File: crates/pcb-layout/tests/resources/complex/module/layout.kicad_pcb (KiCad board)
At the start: 2 copper layers, 4 parts

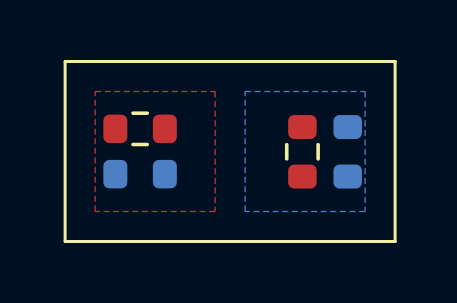
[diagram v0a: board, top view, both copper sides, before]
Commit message: add more interesting test
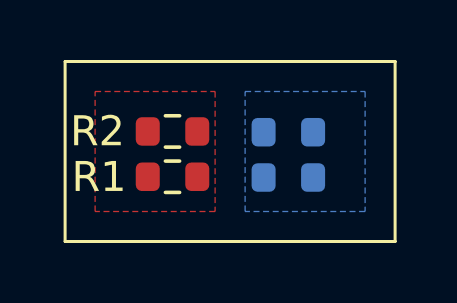
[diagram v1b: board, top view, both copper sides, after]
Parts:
- R1: moved to F.Cu
- R4: moved to B.Cu
- moved R3 2.16 mm to (153.4, 105.9), turned to 180 degrees
- moved R1 1.08 mm to (149.6, 105.8)
- moved R2 1.08 mm to (149.6, 104.3)
- moved R4 0.80 mm to (153.4, 104.4), turned to 180 degrees

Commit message: add zone sync
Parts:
- moved R3 27.5 mm to (176.1, 90.3)
- moved R1 27.5 mm to (172.2, 90.3)
- moved R2 27.5 mm to (172.2, 88.8)
- moved R4 27.5 mm to (176.1, 88.8)
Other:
- board text added: "HELLO"
- board text added: "WORLD"
